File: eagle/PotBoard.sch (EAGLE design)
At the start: 29 parts, among them IC1 MEGA8-AI, Q1 20MHz, Q3 IRLML5203, X1 MICROMATCH-8SMD

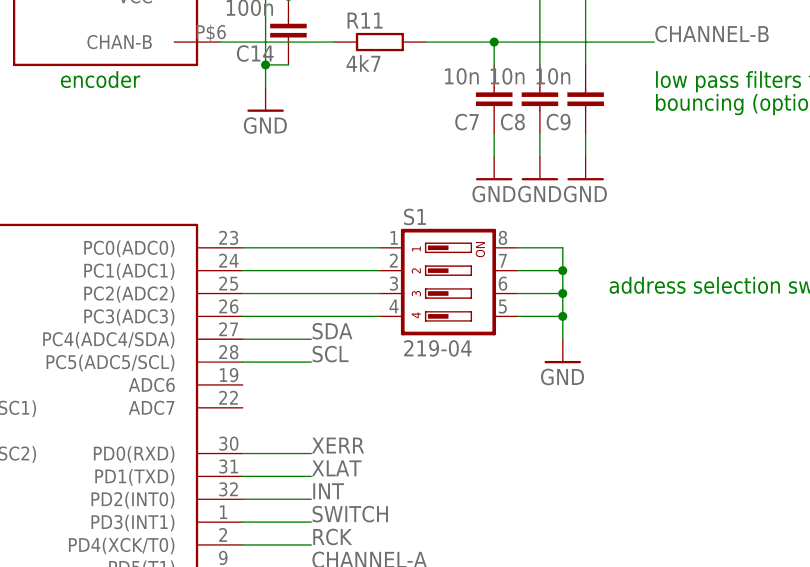
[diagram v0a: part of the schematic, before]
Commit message: Removed a stupid error from the pcbs and included an instructions file. Switched the firmware to use just two switches instead of four. No one's gonna build an arc16 anyway.
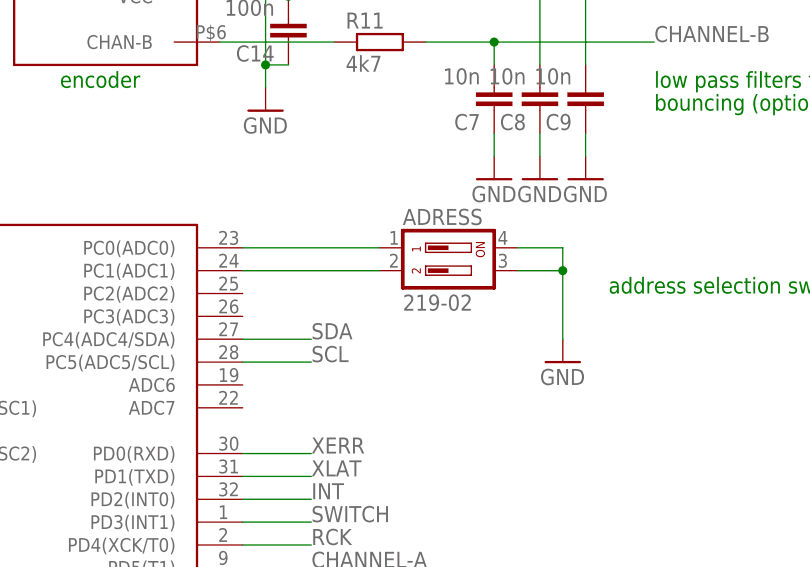
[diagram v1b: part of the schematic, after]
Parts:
- removed S1: 219-04, switch-dil:219-04
- added ADRESS: 219-02, switch-dil:219-02
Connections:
- removed net N$22: IC1.PC2(ADC2), S1.3
- removed net N$23: IC1.PC3(ADC3), S1.4
- net GND: now also ADRESS.3, ADRESS.4; no longer S1.5, S1.6, S1.7, S1.8
- net N$20: now also ADRESS.2; no longer S1.2
- net N$6: now also ADRESS.1; no longer S1.1
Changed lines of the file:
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@@
 <part name="+3V7" library="supply1" deviceset="+3V3" device=""/>
 <part name="JP4" library="pinhead-2" deviceset="PINHD-2X5" device="_2.54-SMD"/>
-<part name="S1" library="switch-dil" deviceset="219-04*" device="">
-<attribute name="MF" value=""/>
-<attribute name="MPN" value=""/>
-<attribute name="OC_FARNELL" value="unknown"/>
-<attribute name="OC_NEWARK" value="unknown"/>
-</part>
 <part name="R2" library="rcl" deviceset="R-EU_" device="R0603" value="330"/>
 <part name="R3" library="rcl" deviceset="R-EU_" device="R0603" value="330"/>
@@
 <part name="R5" library="rcl" deviceset="R-EU_" device="R0603" value="10k"/>
 <part name="X1" library="con-amp-micromatch-2" deviceset="MICROMATCH-8" device="SMD"/>
+<part name="ADRESS" library="switch-dil" deviceset="219-02*" device=""/>
 </parts>
 <sheets>
@@
 <instance part="+3V7" gate="G$1" x="-88.9" y="60.96"/>
 <instance part="JP4" gate="A" x="-101.6" y="45.72" rot="MR180"/>
-<instance part="S1" gate="G$1" x="66.04" y="76.2" rot="R270"/>
 <instance part="R2" gate="G$1" x="-48.26" y="58.42"/>
 <instance part="R3" gate="G$1" x="-48.26" y="43.18"/>
@@
 <instance part="X1" gate="-7" x="-78.74" y="83.82"/>
 <instance part="X1" gate="-8" x="-78.74" y="81.28"/>
+<instance part="ADRESS" gate="G$1" x="66.04" y="78.74" rot="R270"/>
 </instances>
 <busses>
@@
 <wire x1="73.66" y1="78.74" x2="78.74" y2="78.74" width="0.1524" layer="91"/>
 <wire x1="78.74" y1="78.74" x2="78.74" y2="76.2" width="0.1524" layer="91"/>
-<wire x1="78.74" y1="76.2" x2="78.74" y2="73.66" width="0.1524" layer="91"/>
-<wire x1="73.66" y1="71.12" x2="78.74" y2="71.12" width="0.1524" layer="91"/>
-<wire x1="73.66" y1="73.66" x2="78.74" y2="73.66" width="0.1524" layer="91"/>
-<wire x1="78.74" y1="73.66" x2="78.74" y2="71.12" width="0.1524" layer="91"/>
-<junction x="78.74" y="71.12"/>
-<wire x1="78.74" y1="71.12" x2="78.74" y2="68.58" width="0.1524" layer="91"/>
-<junction x="78.74" y="73.66"/>
+<wire x1="78.74" y1="76.2" x2="78.74" y2="68.58" width="0.1524" layer="91"/>
 <junction x="78.74" y="76.2"/>
-<pinref part="S1" gate="G$1" pin="5"/>
-<pinref part="S1" gate="G$1" pin="6"/>
-<pinref part="S1" gate="G$1" pin="7"/>
-<pinref part="S1" gate="G$1" pin="8"/>
+<pinref part="ADRESS" gate="G$1" pin="3"/>
+<pinref part="ADRESS" gate="G$1" pin="4"/>
 </segment>
 <segment>
@@
 <pinref part="IC1" gate="G$1" pin="PC0(ADC0)"/>
 <wire x1="58.42" y1="78.74" x2="43.18" y2="78.74" width="0.1524" layer="91"/>
-<pinref part="S1" gate="G$1" pin="1"/>
+<pinref part="ADRESS" gate="G$1" pin="1"/>
 </segment>
 </net>
@@
 <pinref part="IC1" gate="G$1" pin="PC1(ADC1)"/>
 <wire x1="58.42" y1="76.2" x2="43.18" y2="76.2" width="0.1524" layer="91"/>
-<pinref part="S1" gate="G$1" pin="2"/>
-</segment>
-</net>
-<net name="N$22" class="0">
-<segment>
-<pinref part="IC1" gate="G$1" pin="PC2(ADC2)"/>
-<wire x1="58.42" y1="73.66" x2="43.18" y2="73.66" width="0.1524" layer="91"/>
-<pinref part="S1" gate="G$1" pin="3"/>
-</segment>
-</net>
-<net name="N$23" class="0">
-<segment>
-<pinref part="IC1" gate="G$1" pin="PC3(ADC3)"/>
-<wire x1="58.42" y1="71.12" x2="43.18" y2="71.12" width="0.1524" layer="91"/>
-<pinref part="S1" gate="G$1" pin="4"/>
-</segment>
-</net>
+<pinref part="ADRESS" gate="G$1" pin="2"/>
+</segment>
+</net>
